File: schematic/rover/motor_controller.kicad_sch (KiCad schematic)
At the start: 9 parts, among them U3 Pico, U5 ACS711xEXLT-31AB, U7 ACS711xEXLT-31AB

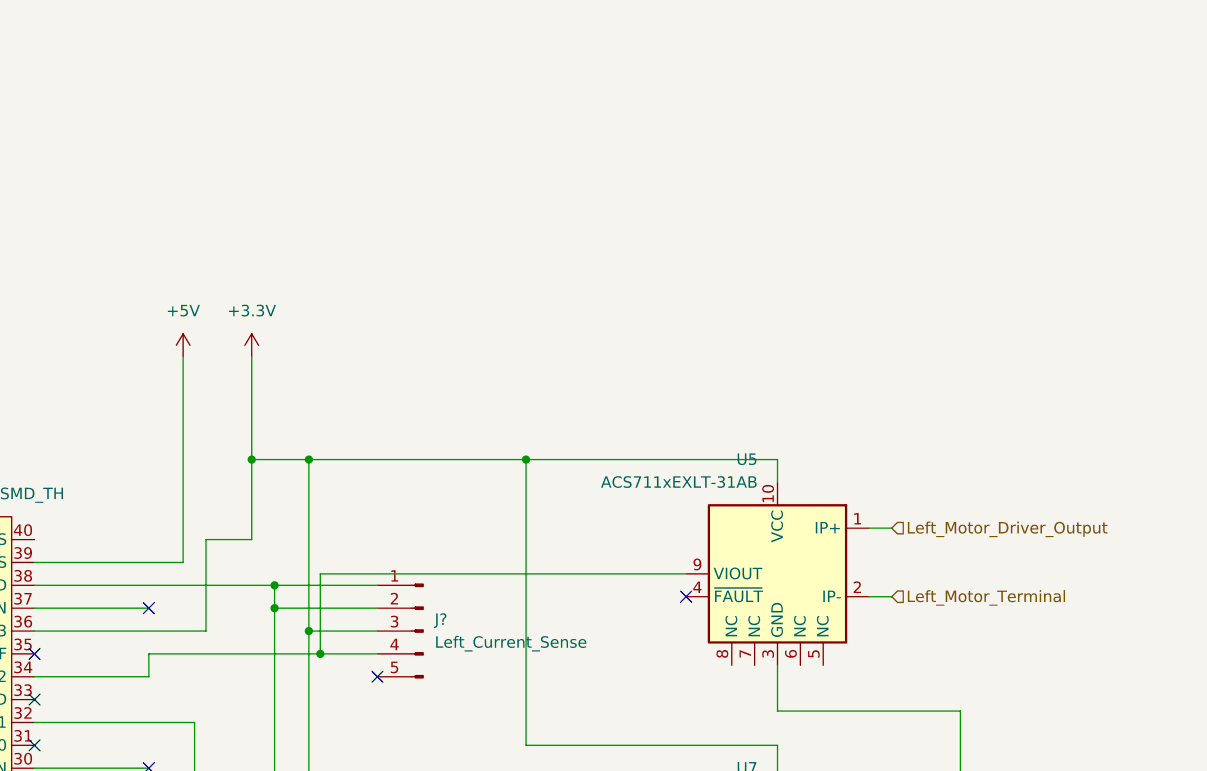
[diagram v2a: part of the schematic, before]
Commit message: Complete power board and motor wiring
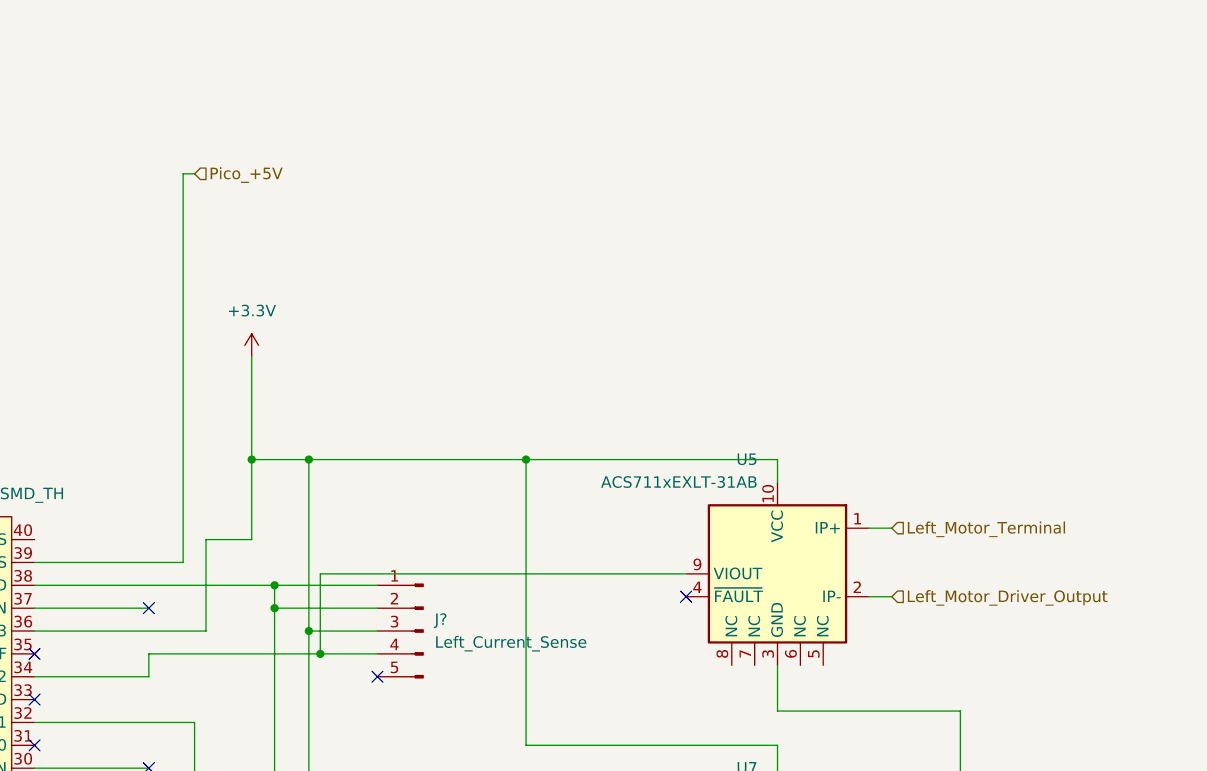
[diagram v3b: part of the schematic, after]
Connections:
- net +5V: no longer U3.39 (VSYS)
- net Left_Motor_Driver_Output: now also U5.2 (IP-); no longer U5.1 (IP+)
- net Left_Motor_Terminal: now also U5.1 (IP+); no longer U5.2 (IP-)
- new net Pico_+5V: U3.39 (VSYS)
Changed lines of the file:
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@@
+    (stroke (width 0) (type default))
+  )
+  (wire (pts (xy 149.86 38.1) (xy 151.13 38.1))
     (stroke (width 0) (type default))
   )
@@
     (stroke (width 0) (type default))
   )
-  (wire (pts (xy 149.86 58.42) (xy 149.86 81.28))
+  (wire (pts (xy 149.86 38.1) (xy 149.86 81.28))
     (stroke (width 0) (type default))
   )
@@
     (effects (font (size 1.27 1.27)) (justify left))
   )
+  (hierarchical_label "Pico_+5V" (shape input) (at 151.13 38.1 0) (fields_autoplaced)
+    (effects (font (size 1.27 1.27)) (justify left))
+  )
   (hierarchical_label "Right_Motor_Terminal" (shape input) (at 228.6 119.38 0) (fields_autoplaced)
     (effects (font (size 1.27 1.27)) (justify left))
@@
     (effects (font (size 1.27 1.27)) (justify left))
   )
-  (hierarchical_label "Left_Motor_Terminal" (shape input) (at 228.6 85.09 0) (fields_autoplaced)
-    (effects (font (size 1.27 1.27)) (justify left))
-  )
   (hierarchical_label "Central_Hub__RX" (shape input) (at 58.42 67.31 0) (fields_autoplaced)
     (effects (font (size 1.27 1.27)) (justify left))
@@
     (effects (font (size 1.27 1.27)) (justify left))
   )
+  (hierarchical_label "Left_Motor_Terminal" (shape input) (at 228.6 77.47 0) (fields_autoplaced)
+    (effects (font (size 1.27 1.27)) (justify left))
+  )
   (hierarchical_label "OUTA_Right__Blue" (shape input) (at 33.02 181.61 0) (fields_autoplaced)
     (effects (font (size 1.27 1.27)) (justify left))
@@
     (effects (font (size 1.27 1.27)) (justify right))
   )
-  (hierarchical_label "Left_Motor_Driver_Output" (shape input) (at 228.6 77.47 0) (fields_autoplaced)
-    (effects (font (size 1.27 1.27)) (justify left))
-  )
   (hierarchical_label "Central_Hub__RX" (shape input) (at 96.52 93.98 180) (fields_autoplaced)
     (effects (font (size 1.27 1.27)) (justify right))
+  )
+  (hierarchical_label "Left_Motor_Driver_Output" (shape input) (at 228.6 85.09 0) (fields_autoplaced)
+    (effects (font (size 1.27 1.27)) (justify left))
   )
   (hierarchical_label "OUTA_Left__Blue" (shape input) (at 39.37 64.77 180) (fields_autoplaced)
@@
         )
       )
-    )
-  )
-  (symbol (lib_id "power:+5V") (at 149.86 58.42 0) (unit 1)
-    (in_bom yes) (on_board yes) (dnp no) (fields_autoplaced)
-    (property "Reference" "#PWR?" (at 149.86 62.23 0)
-      (effects (font (size 1.27 1.27)) hide)
-    )
-    (property "Value" "+5V" (at 149.86 53.34 0)
-      (effects (font (size 1.27 1.27)))
-    )
-    (property "Footprint" "" (at 149.86 58.42 0)
-      (effects (font (size 1.27 1.27)) hide)
-    )
-    (property "Datasheet" "" (at 149.86 58.42 0)
-      (effects (font (size 1.27 1.27)) hide)
-    )
-    (pin "1")
-    (instances
-      (project "rover"
-        (path "/e69e2e1e-a9af-4127-a558-2cc8fb636c94"
-          (reference "#PWR?") (unit 1)
-        )
-        (path "/e69e2e1e-a9af-4127-a558-2cc8fb636c94/8350866f-b296-4194-b8e5-2cec92f34e35/287896c2-ba29-4646-9325-bc5db50cda10"
-          (reference "#PWR013") (unit 1)
-        )
-        (path "/e69e2e1e-a9af-4127-a558-2cc8fb636c94/8350866f-b296-4194-b8e5-2cec92f34e35/47de232d-0f73-4c94-9f7d-6f96c0485431"
-          (reference "#PWR019") (unit 1)
-        )
-      )
